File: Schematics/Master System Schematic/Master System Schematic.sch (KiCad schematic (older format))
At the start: 40 parts, among them J1 GND, J10 +12V, J11 Charger +12V, J2 TS+, J3 TS-, J8 Charger GND, K12 Cooling Pump Relay, M1 Cooling Pump, SW1 GLVMS, SW10 SMD, SW11 BRAKE_SWITCH, SW12 SW_SPST_Pressure, SW13 SW_SPST_Pressure, SW2 SideMounted (BRB), SW3 SideMounted (BRB), SW4 Brake Over-Travel Switch, SW5 Latching Circuit Reset, SW6 Cockpit Shutdown (BRB), SW7 TSMS, SW8 SMD, SW9 HVD, U3 FuseBox_PSZACCEPS052H, U4 Bender_Isometer_IR155-3204, U6 RinehartPM100DX_MotorControll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, U7 Emrax228HV_Motor

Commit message: Had to refactor all IDs
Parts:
- renumbered BT505 to BT1, D8 to D6, J10 to J1, J11 to J2, J1 to J3, J8 to J4, J2 to J5, J3 to J6, K12 to K1, R5 to R1, SW3 to SW1, SW1 to SW3, U3 to U1, U4 to U2, U6 to U3, U7 to U4
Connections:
- new net: U1.6, U3.23 (CANB_H), U3.8 (Reverse_Enable_Switch)
- new net: U3.~ (TS-), U4.~ (AC3) (x2)
- now unconnected: U3.23 (CANB_H), U3.8 (Reverse_Enable_Switch)
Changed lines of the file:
@@
 $Descr B 17000 11000
 encoding utf-8
-Sheet 1 17
+Sheet 1 21
 Title "NER FH 2020-2021 Master Electrical Schematic"
 Date "2020-10-12"
@@
 P 1250 7650
 AR Path="/5F45AFB3/5F633A5B" Ref="BT?"  Part="1"
-AR Path="/5F633A5B" Ref="BT505"  Part="1"
-F 0 "BT505" H 1600 7750 50  0000 L CNN
+AR Path="/5F633A5B" Ref="BT1"  Part="1"
+F 0 "BT1" H 1600 7750 50  0000 L CNN
 F 1 "12V GLV Battery" H 1400 7650 50  0000 L CNN
 F 2 "" V 1250 7710 50  0001 C CNN
@@
 P 1250 4700
 AR Path="/5F45AFB3/5F633A6E" Ref="SW?"  Part="1"
-AR Path="/5F633A6E" Ref="SW3"  Part="1"
-F 0 "SW3" V 1200 5250 50  0000 R CNN
+AR Path="/5F633A6E" Ref="SW1"  Part="1"
+F 0 "SW1" V 1200 5250 50  0000 R CNN
 F 1 "SideMounted (BRB)" V 1300 5550 50  0000 R CNN
 F 2 "" H 1250 4900 50  0001 C CNN
@@
 P 1250 6100
 AR Path="/5F45AFB3/5F633A74" Ref="SW?"  Part="1"
-AR Path="/5F633A74" Ref="SW1"  Part="1"
-F 0 "SW1" V 1250 5700 50  0000 L CNN
+AR Path="/5F633A74" Ref="SW3"  Part="1"
+F 0 "SW3" V 1250 5700 50  0000 L CNN
 F 1 "GLVMS" V 1350 5650 50  0000 L CNN
 F 2 "" H 1250 6100 50  0001 C CNN
@@
 $EndComp
 $Comp
-L NER:Bender_Isometer_IR155-3204 U4
+L NER:Bender_Isometer_IR155-3204 U2
 U 1 1 5F94A015
 P 7600 3800
-F 0 "U4" H 7600 3915 50  0000 C CNN
+F 0 "U2" H 7600 3915 50  0000 C CNN
 F 1 "Bender_Isometer_IR155-3204" H 7600 3824 50  0000 C CNN
 F 2 "" H 7600 3800 50  0001 C CNN
@@
 	6550 2150 6550 1950
 $Comp
-L Device:R R5
+L Device:R R1
 U 1 1 5F4E06AE
 P 7600 3500
-F 0 "R5" V 7807 3500 50  0000 C CNN
+F 0 "R1" V 7807 3500 50  0000 C CNN
 F 1 "2.2k" V 7716 3500 50  0000 C CNN
 F 2 "" V 7530 3500 50  0001 C CNN
@@
 	6200 5000 5950 5000
 $Comp
-L Connector:Conn_01x01_Female J3
+L Connector:Conn_01x01_Female J6
 U 1 1 5FB0713A
 P 5850 9350
-F 0 "J3" V 5750 9200 50  0000 L CNN
+F 0 "J6" V 5750 9200 50  0000 L CNN
 F 1 "TS-" V 5650 9150 50  0000 L CNN
 F 2 "" H 5850 9350 50  0001 C CNN
@@
 $EndComp
 $Comp
-L Connector:Conn_01x01_Female J2
+L Connector:Conn_01x01_Female J5
 U 1 1 5FB022E4
 P 5550 9350
-F 0 "J2" V 5450 9200 50  0000 L CNN
+F 0 "J5" V 5450 9200 50  0000 L CNN
 F 1 "TS+" V 5350 9150 50  0000 L CNN
 F 2 "" H 5550 9350 50  0001 C CNN
@@
 $EndComp
 $Comp
-L Connector:Conn_01x01_Female J1
+L Connector:Conn_01x01_Female J3
 U 1 1 5FAE402D
 P 3950 9350
-F 0 "J1" V 3850 9200 50  0000 L CNN
+F 0 "J3" V 3850 9200 50  0000 L CNN
 F 1 "GND" V 3750 9150 50  0000 L CNN
 F 2 "" H 3950 9350 50  0001 C CNN
@@
 CHASSIS_GND
 $Comp
-L NER:FuseBox_PSZACCEPS052H U3
+L NER:FuseBox_PSZACCEPS052H U1
 U 1 1 5F6D724E
 P 1250 3250
-F 0 "U3" H 1250 3415 50  0000 C CNN
+F 0 "U1" H 1250 3415 50  0000 C CNN
 F 1 "FuseBox_PSZACCEPS052H" H 1250 3324 50  0000 C CNN
 F 2 "" H 1250 3400 50  0001 C CNN
@@
 	15350 1000 15350 7900
 $Comp
-L NER:RinehartPM100DX_MotorController U6
+L NER:RinehartPM100DX_MotorController U3
 U 1 1 5F97D518
 P 14300 8350
-F 0 "U6" H 14300 8515 50  0000 C CNN
+F 0 "U3" H 14300 8515 50  0000 C CNN
 F 1 "RinehartPM100DX_MotorController" H 14300 8424 50  0000 C CNN
 F 2 "" H 14300 8350 50  0001 C CNN
@@
 	15750 8250 15750 8300
 $Comp
-L NER:Emrax228HV_Motor U7
+L NER:Emrax228HV_Motor U4
 U 1 1 5F972C2B
 P 16100 7800
-F 0 "U7" H 16050 7950 50  0000 L CNN
+F 0 "U4" H 16050 7950 50  0000 L CNN
 F 1 "Emrax228HV_Motor" H 15750 7850 50  0000 L CNN
 F 2 "" H 16100 7800 50  0001 C CNN
@@
 	9450 2300 9350 2300
 $Comp
-L NER:ST-R10_LED D8
+L NER:ST-R10_LED D6
 U 1 1 5F87123F
 P 9200 2800
-F 0 "D8" H 9175 3031 50  0000 C CNN
+F 0 "D6" H 9175 3031 50  0000 C CNN
 F 1 "ST-R10_LED" H 9175 2940 50  0000 C CNN
 F 2 "" H 9150 2800 50  0001 C CNN
@@
 	8900 2800 9000 2800
 $Comp
-L Connector:Conn_01x01_Male J8
+L Connector:Conn_01x01_Male J4
 U 1 1 5F89DD3D
 P 3950 9750
-F 0 "J8" V 4012 9794 50  0000 L CNN
+F 0 "J4" V 4012 9794 50  0000 L CNN
 F 1 "Charger GND" V 4103 9794 50  0000 L CNN
 F 2 "" H 3950 9750 50  0001 C CNN
@@
 $EndComp
 $Comp
-L Connector:Conn_01x01_Male J11
+L Connector:Conn_01x01_Male J2
 U 1 1 5F8D4529
 P 3650 9750
-F 0 "J11" V 3700 9550 50  0000 L CNN
+F 0 "J2" V 3700 9550 50  0000 L CNN
 F 1 "Charger +12V" V 3800 9100 50  0000 L CNN
 F 2 "" H 3650 9750 50  0001 C CNN
@@
 $EndComp
 $Comp
-L Connector:Conn_01x01_Female J10
+L Connector:Conn_01x01_Female J1
 U 1 1 5F93092A
 P 3650 9350
-F 0 "J10" V 3550 9200 50  0000 L CNN
+F 0 "J1" V 3550 9200 50  0000 L CNN
 F 1 "+12V" V 3450 9150 50  0000 L CNN
 F 2 "" H 3650 9350 50  0001 C CNN
@@
 	1250 5750 1250 5900
 $Comp
-L Relay:DIPxx-1Axx-11x K12
+L Relay:DIPxx-1Axx-11x K1
 U 1 1 5F9B5A7A
 P 2950 5550
-F 0 "K12" V 2383 5550 50  0000 C CNN
+F 0 "K1" V 2383 5550 50  0000 C CNN
 F 1 "Cooling Pump Relay" V 2474 5550 50  0000 C CNN
 F 2 "Relay_THT:Relay_StandexMeder_DIP_LowProfile" H 3300 5500 50  0001 L CNN

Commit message: Fixed Driver IO and annotations
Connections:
- new net: U1.6, U3.23 (CANB_H), U3.8 (Reverse_Enable_Switch)
- new net: U3.~ (TS-), U4.~ (AC3) (x2)
- now unconnected: U3.23 (CANB_H), U3.8 (Reverse_Enable_Switch)
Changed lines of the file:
@@
 EESchema Schematic File Version 4
-LIBS:Master System Schematic-cache
 EELAYER 30 0
 EELAYER END

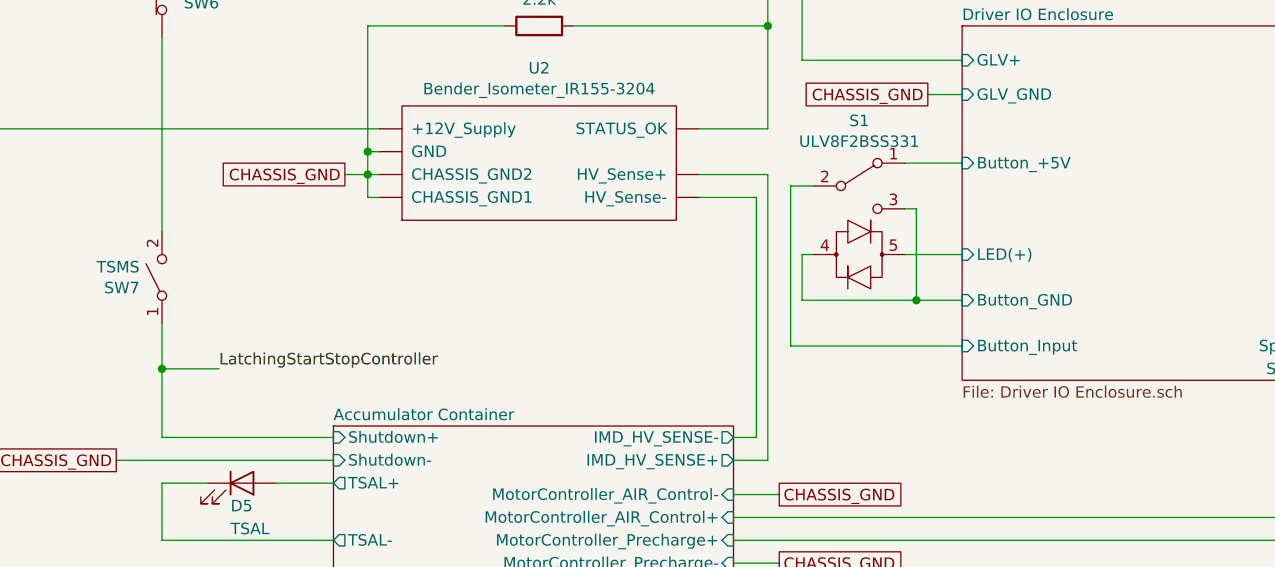
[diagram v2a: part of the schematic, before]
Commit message: Added Master Schematic Wiring
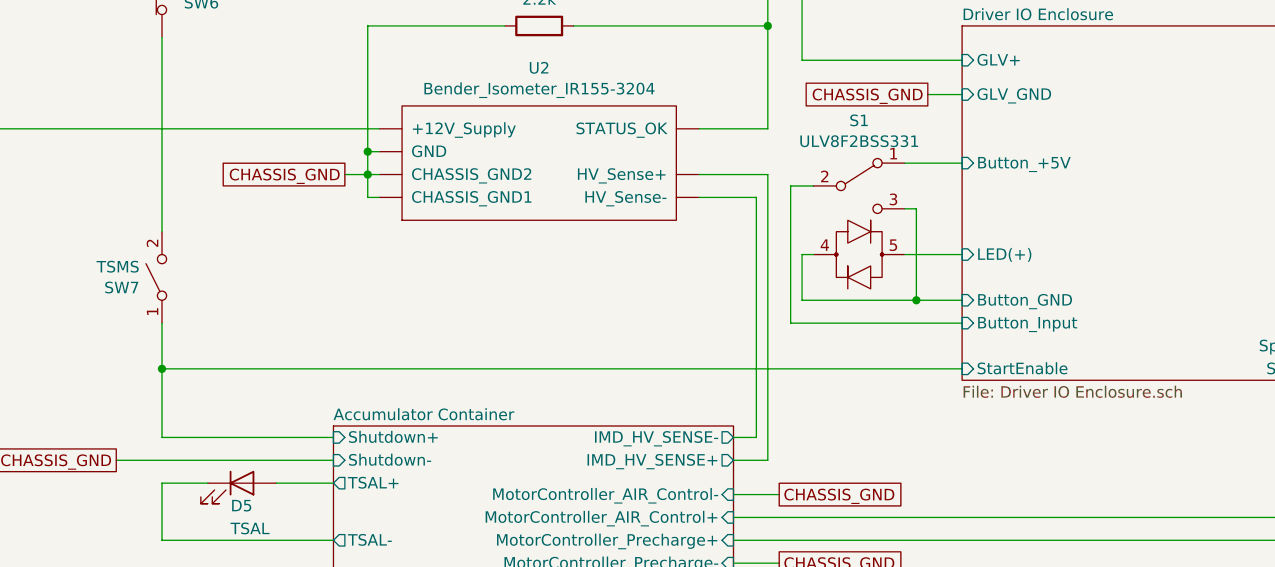
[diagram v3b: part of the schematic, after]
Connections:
- net LatchingStartStopController renamed Accumulator Container/Shutdown+
- new net: U1.6, U3.23 (CANB_H), U3.8 (Reverse_Enable_Switch)
- new net: U3.~ (TS-), U4.~ (AC3) (x2)
- now unconnected: U3.23 (CANB_H), U3.8 (Reverse_Enable_Switch)
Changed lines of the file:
@@
 EESchema Schematic File Version 4
+LIBS:Master System Schematic-cache
 EELAYER 30 0
 EELAYER END
@@
 Text GLabel 1400 7900 2    50   UnSpc ~ 0
 CHASSIS_GND
-Text Label 6200 5000 0    50   ~ 0
-LatchingStartStopController
 Text GLabel 6650 2150 2    50   UnSpc ~ 0
 CHASSIS_GND
@@
 Wire Wire Line
 	1250 4900 1250 5250
-Wire Wire Line
-	6200 5000 5950 5000
 $Comp
 L Connector:Conn_01x01_Female J6
@@
 F6 "LED(+)" I L 9450 4500 50
 F7 "Button_GND" I L 9450 4700 50
-F8 "Button_Input" I L 9450 4900 50
+F8 "Button_Input" I L 9450 4800 50
 F9 "Button_+5V" I L 9450 4100 50
 F10 "Speaker+" I R 11150 4900 50
 F11 "Speaker-" I R 11150 5000 50
+F12 "StartEnable" I L 9450 5000 50
 $EndSheet
 Text GLabel 15200 7250 1    50   UnSpc ~ 0
@@
 	9200 4300 9250 4300
 Wire Wire Line
-	9450 4900 8700 4900
+	9450 4800 8700 4800
 Wire Wire Line
 	8700 4200 8800 4200
@@
 CHASSIS_GND
 Wire Wire Line
-	8700 4200 8700 4900
+	8700 4200 8700 4800
 Wire Wire Line
 	9200 4100 9450 4100
@@
 Wire Wire Line
 	12750 3250 12950 3250
+Wire Wire Line
+	5950 5000 9450 5000
 Wire Bus Line
 	11300 3250 11300 3600

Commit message: Fixed Driver IO LED Voltage Divider
Added voltage divider to LED to bring 5v down to 3v.
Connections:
- new net: U1.6, U3.23 (CANB_H), U3.8 (Reverse_Enable_Switch)
- new net: U3.~ (TS-), U4.~ (AC3) (x2)
- now unconnected: U3.23 (CANB_H), U3.8 (Reverse_Enable_Switch)
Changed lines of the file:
@@
 EESchema Schematic File Version 4
-LIBS:Master System Schematic-cache
 EELAYER 30 0
 EELAYER END

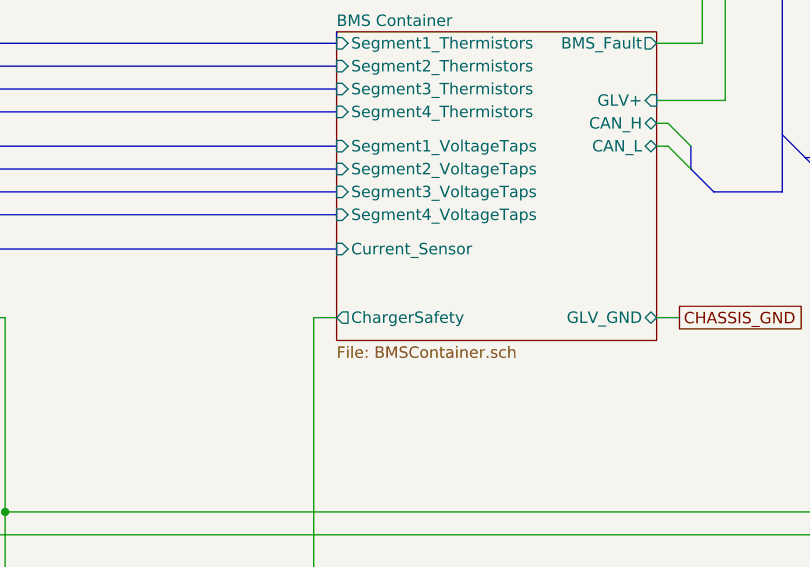
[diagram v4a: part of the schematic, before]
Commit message: Added Charger Power pin to BMS schem
Pulled charger power pin through to master sheet.
Not implemented because I'm not sure how david will be doing this
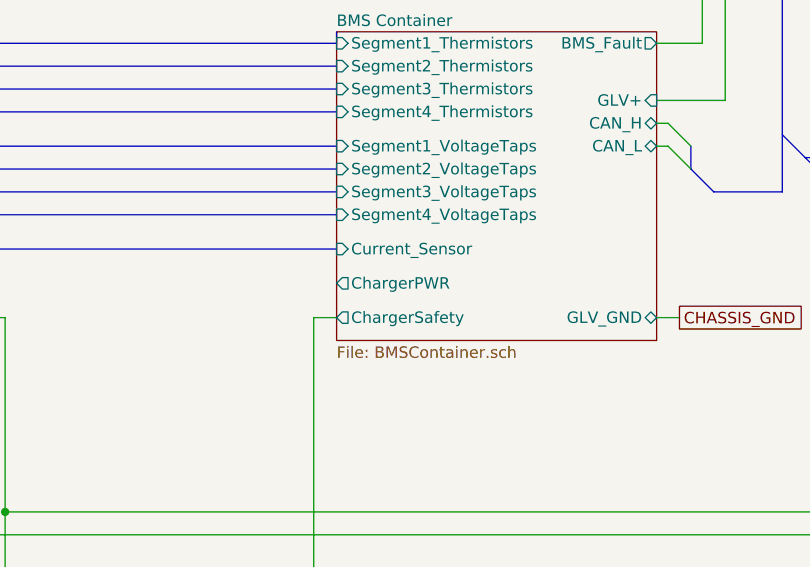
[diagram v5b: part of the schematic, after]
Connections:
- new net: U1.6, U3.23 (CANB_H), U3.8 (Reverse_Enable_Switch)
- new net: U3.~ (TS-), U4.~ (AC3) (x2)
- now unconnected: U3.23 (CANB_H), U3.8 (Reverse_Enable_Switch)
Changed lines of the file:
@@
 F15 "CAN_L" B R 11500 6550 50
 F16 "ChargerSafety" O L 10100 7300 50
+F17 "ChargerPWR" O L 10100 7150 50
 $EndSheet
 Text GLabel 4100 8500 2    50   UnSpc ~ 0

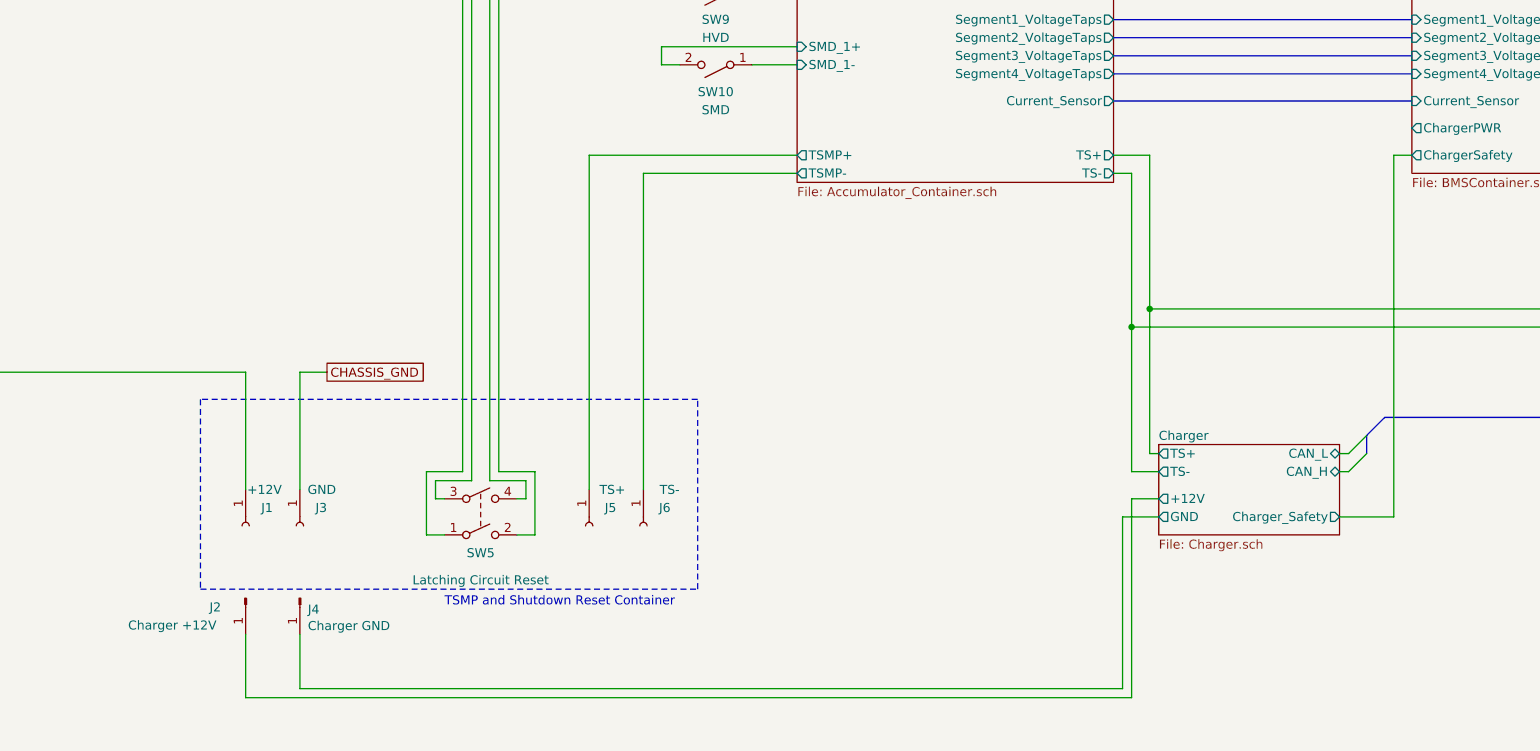
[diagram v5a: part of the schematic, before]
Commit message: Added Connector for BMS Charge 12V
Added connector and wire run for how I currently imagine it will work. Requires a new plug in the TSMP enclosure
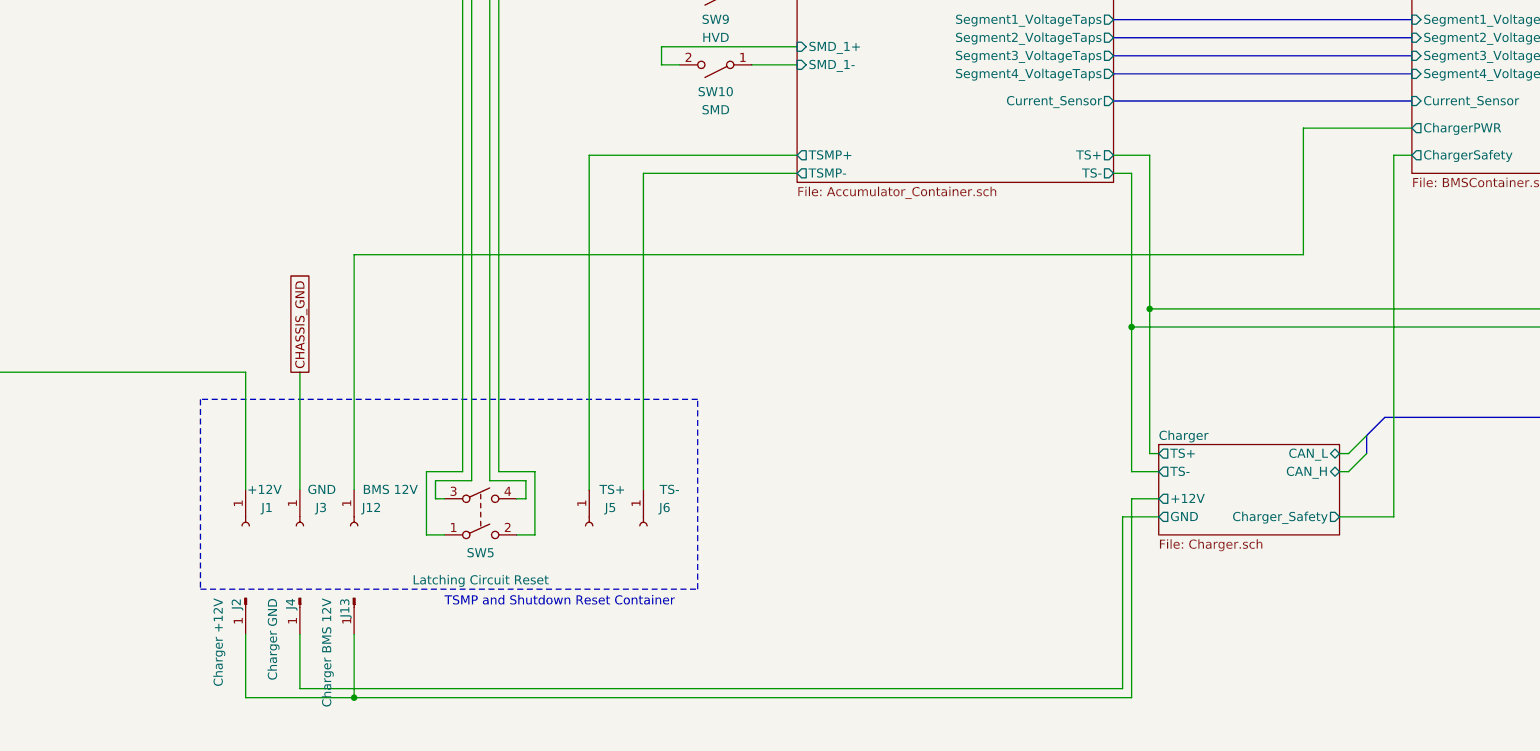
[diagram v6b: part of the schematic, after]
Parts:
- added J12: BMS 12V, symbol Connector:Conn_01x01_Female
- added J13: Charger BMS 12V, symbol Connector:Conn_01x01_Male
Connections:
- net BMS Container/ChargerPWR: now also J12.1 (Pin_1)
- net Charger/+12V: now also J13.1 (Pin_1)
- new net: U1.6, U3.23 (CANB_H), U3.8 (Reverse_Enable_Switch)
- new net: U3.~ (TS-), U4.~ (AC3) (x2)
- now unconnected: U3.23 (CANB_H), U3.8 (Reverse_Enable_Switch)
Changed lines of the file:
@@
 EESchema Schematic File Version 4
+LIBS:Master System Schematic-cache
 EELAYER 30 0
 EELAYER END
@@
 F17 "ChargerPWR" O L 10100 7150 50
 $EndSheet
-Text GLabel 4100 8500 2    50   UnSpc ~ 0
+Text GLabel 3950 8500 1    50   UnSpc ~ 0
 CHASSIS_GND
 $Comp
@@
 U 1 1 5F89DD3D
 P 3950 9750
-F 0 "J4" V 4012 9794 50  0000 L CNN
-F 1 "Charger GND" V 4103 9794 50  0000 L CNN
+F 0 "J4" H 3950 9700 50  0000 L CNN
+F 1 "Charger GND" H 3950 9600 50  0000 L CNN
 F 2 "" H 3950 9750 50  0001 C CNN
 F 3 "~" H 3950 9750 50  0001 C CNN
@@
 U 1 1 5F8D4529
 P 3650 9750
-F 0 "J2" V 3700 9550 50  0000 L CNN
-F 1 "Charger +12V" V 3800 9100 50  0000 L CNN
+F 0 "J2" H 3650 9700 50  0000 L CNN
+F 1 "Charger +12V" H 3650 9600 50  0000 L CNN
 F 2 "" H 3650 9750 50  0001 C CNN
 F 3 "~" H 3650 9750 50  0001 C CNN
@@
 	5550 7300 5550 9150
 Wire Wire Line
-	3950 8500 4100 8500
-Wire Wire Line
 	3650 8500 550  8500
 Wire Wire Line
@@
 	3650 9950 3650 10300
 Wire Wire Line
-	3650 10300 8550 10300
+	3650 10300 4250 10300
 Wire Wire Line
 	8550 10300 8550 9200
@@
 Wire Wire Line
 	5950 5000 9450 5000
+Wire Wire Line
+	10100 7150 9500 7150
+Wire Wire Line
+	9500 7150 9500 7850
+Wire Wire Line
+	9500 7850 4250 7850
+Wire Wire Line
+	4250 7850 4250 9150
+$Comp
+L Connector:Conn_01x01_Female J12
+U 1 1 5F968F75
+P 4250 9350
+F 0 "J12" V 4150 9200 50  0000 L CNN
+F 1 "BMS 12V" V 4050 9150 50  0000 C CNN
+F 2 "" H 4250 9350 50  0001 C CNN
+F 3 "~" H 4250 9350 50  0001 C CNN
+	1    4250 9350
+	0    -1   1    0
+$EndComp
+$Comp
+L Connector:Conn_01x01_Male J13
+U 1 1 5F97C76F
+P 4250 9750
+F 0 "J13" H 4250 9700 50  0000 L CNN
+F 1 "Charger BMS 12V" H 4250 9600 50  0000 L CNN
+F 2 "" H 4250 9750 50  0001 C CNN
+F 3 "~" H 4250 9750 50  0001 C CNN
+	1    4250 9750
+	0    1    1    0
+$EndComp
+Wire Wire Line
+	4250 9950 4250 10300
 Wire Bus Line
 	11300 3250 11300 3600
@@
 Wire Bus Line
 	12050 800  12050 6750
+Connection ~ 4250 10300
+Wire Wire Line
+	4250 10300 8550 10300
 $EndSCHEMATC
